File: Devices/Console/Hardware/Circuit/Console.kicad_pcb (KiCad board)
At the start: 2 copper layers, 96.8 x 60 mm, 30 parts, among them J1 AVR-ISP-6, J2 TYPE-C-31-M-12, J3 Conn_01x13, J4 Conn_01x04, J5 Conn_01x04, SW1 PEC11R-4220F-S0012, SW2 PEC11R-4220F-S0012, SW3 PEC11R-4220F-S0012, SW4 PEC11R-4220F-S0012, SW5 SW_Push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

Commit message: Finalize PCB
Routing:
- net BTN3: track 0.00 -> 291.0 mm, vias 0 -> 3
- net RST: track 0.00 -> 197.4 mm, vias 0 -> 6
- net GND: track 0.00 -> 178.3 mm, vias 0 -> 17
- net BTN1: track 0.00 -> 166.3 mm, vias 0 -> 7
- net VCC: track 0.00 -> 156.5 mm, vias 0 -> 8
- net BTN2: track 0.00 -> 151.6 mm, vias 0 -> 4
- net ENC4A: track 0.00 -> 106.2 mm, vias 0 -> 2
- net SCL: track 0.00 -> 101.4 mm, vias 0 -> 4
- net ENC4B: track 0.00 -> 93.7 mm
- net BTN4: track 0.00 -> 91.8 mm, vias 0 -> 5
- net SDA: track 0.00 -> 90.7 mm, vias 0 -> 8
- net ENC3A: track 0.00 -> 81.4 mm, vias 0 -> 2
- net ENC3B: track 0.00 -> 79.7 mm, vias 0 -> 4
- net RX: track 0.00 -> 74.1 mm, vias 0 -> 6
- net ENC2A: track 0.00 -> 67.8 mm, vias 0 -> 2
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- added copper zone on B.Cu, net GND
- added copper zone on F.Cu, net GND
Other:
- board text added: "GHOSCHT - 2021"
- board text added: "v01"

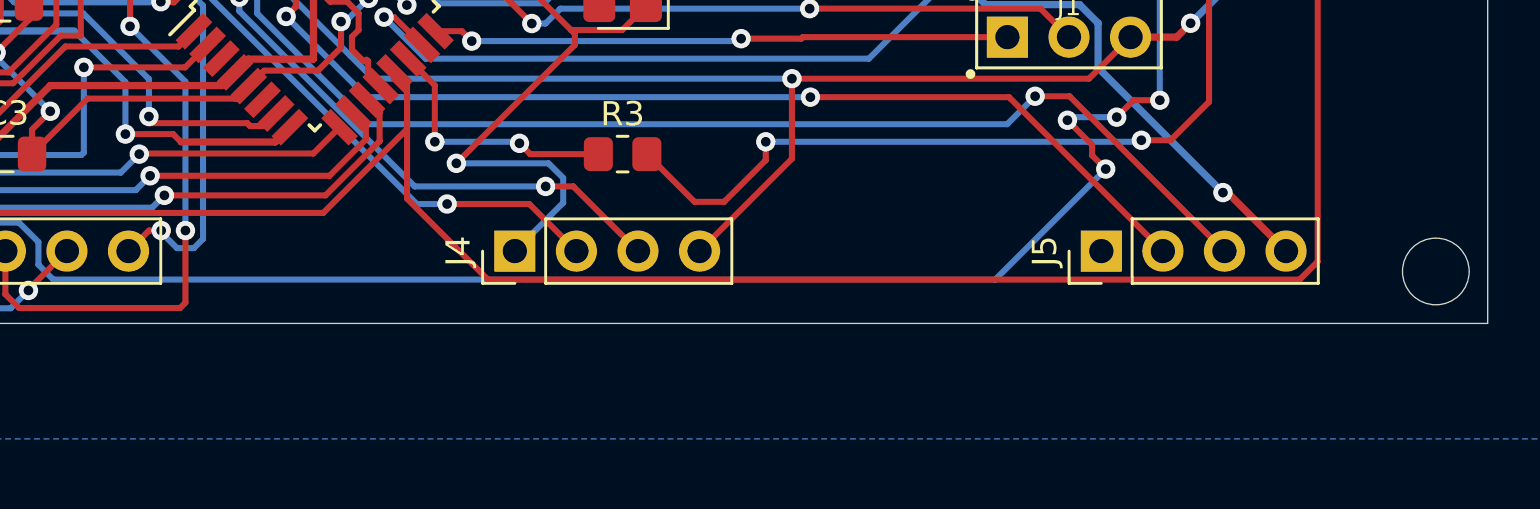
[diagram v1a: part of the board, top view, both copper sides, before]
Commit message: Add breakout pin description
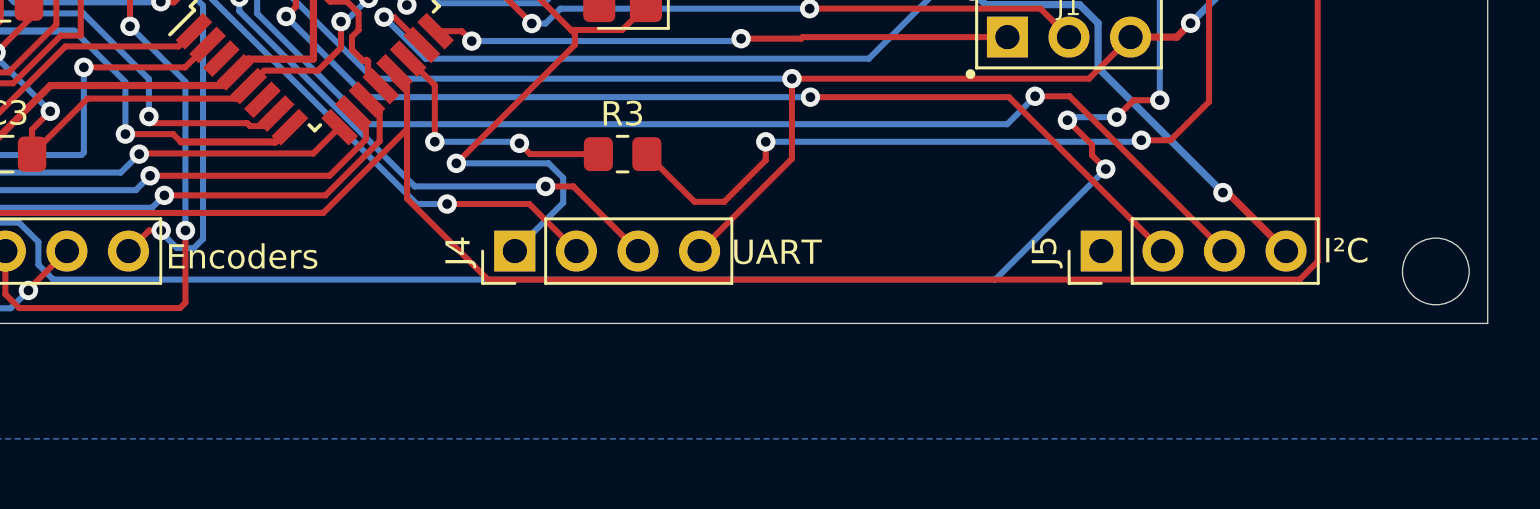
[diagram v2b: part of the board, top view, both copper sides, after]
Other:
- board text added: "Encoders"
- board text added: "I²C"
- board text added: "UART"
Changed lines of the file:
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@@
   (general
     (thickness 1.6)
-    (drawings 15)
+    (drawings 18)
     (tracks 833)
     (zones 0)
@@
     )
   )
+  (gr_text Encoders (at 143.256 122.047) (layer F.SilkS)
+    (effects (font (size 1 1) (thickness 0.15)))
+  )
+  (gr_text UART (at 165.2905 121.8565) (layer F.SilkS)
+    (effects (font (size 1 1) (thickness 0.15)))
+  )
+  (gr_text I²C (at 188.7855 121.793) (layer F.SilkS)
+    (effects (font (size 1 1) (thickness 0.15)))
+  )
   (gr_text "GHOSCHT - 2021" (at 192.913 113.4745 90) (layer B.SilkS)

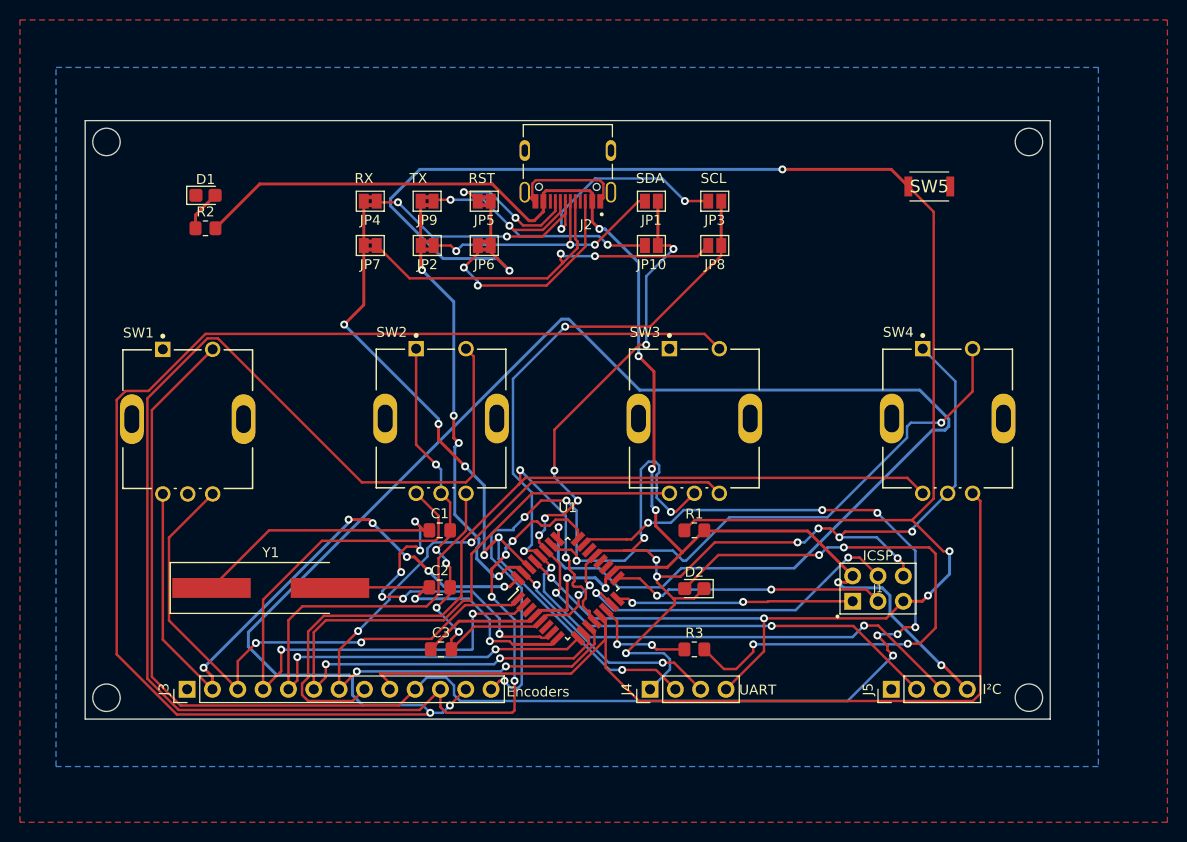
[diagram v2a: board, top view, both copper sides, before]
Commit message: Add proper mounting holes
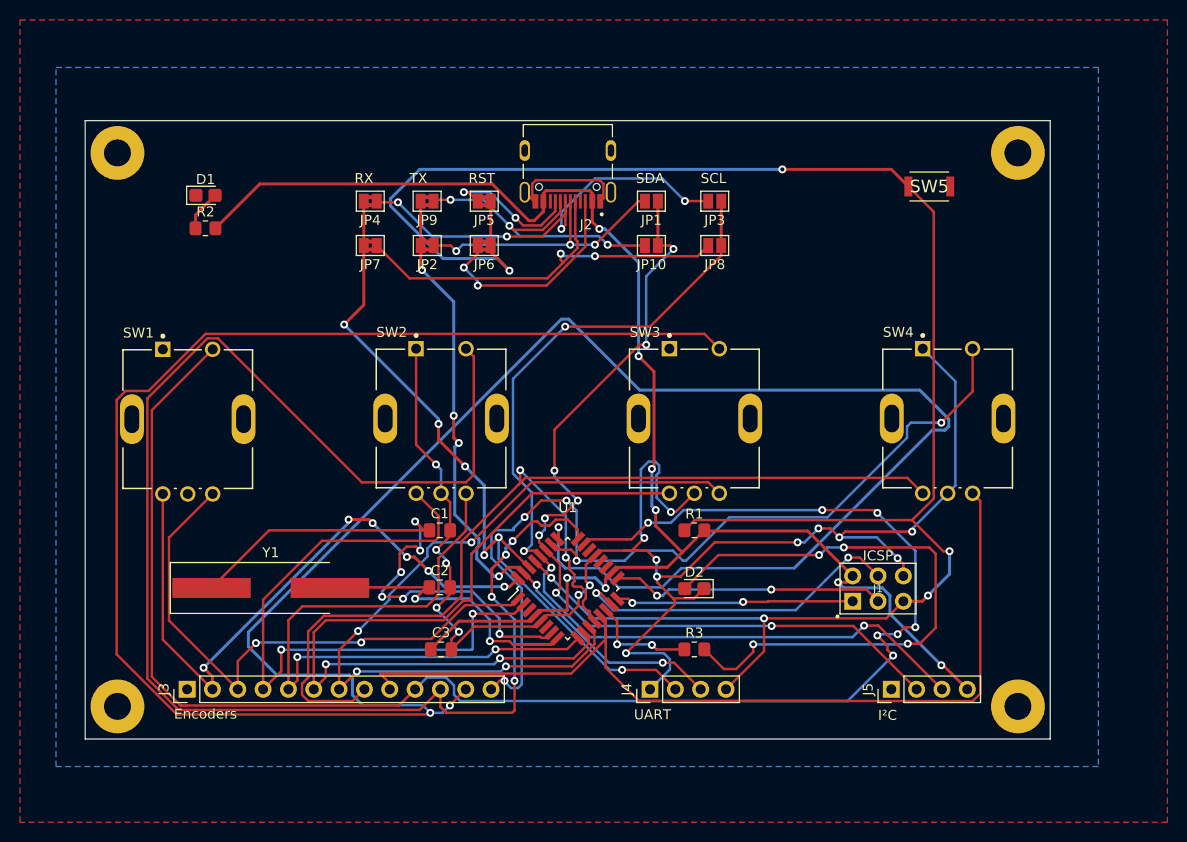
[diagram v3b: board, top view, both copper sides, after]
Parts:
- added PAD1: MountingHole_2.7mm_M2.5_Pad, MountingHole:MountingHole_2.7mm_M2.5_Pad, F.Cu at (101.1, 68.0)
- added PAD2: MountingHole_2.7mm_M2.5_Pad, MountingHole:MountingHole_2.7mm_M2.5_Pad, F.Cu at (191.4, 68.0)
- added PAD3: MountingHole_2.7mm_M2.5_Pad, MountingHole:MountingHole_2.7mm_M2.5_Pad, F.Cu at (101.1, 123.5)
- added PAD4: MountingHole_2.7mm_M2.5_Pad, MountingHole:MountingHole_2.7mm_M2.5_Pad, F.Cu at (191.4, 123.5)
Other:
- board size 96.8 x 60 mm -> 96.8 x 62 mm

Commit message: Improve routing with freerouting + manual fixes
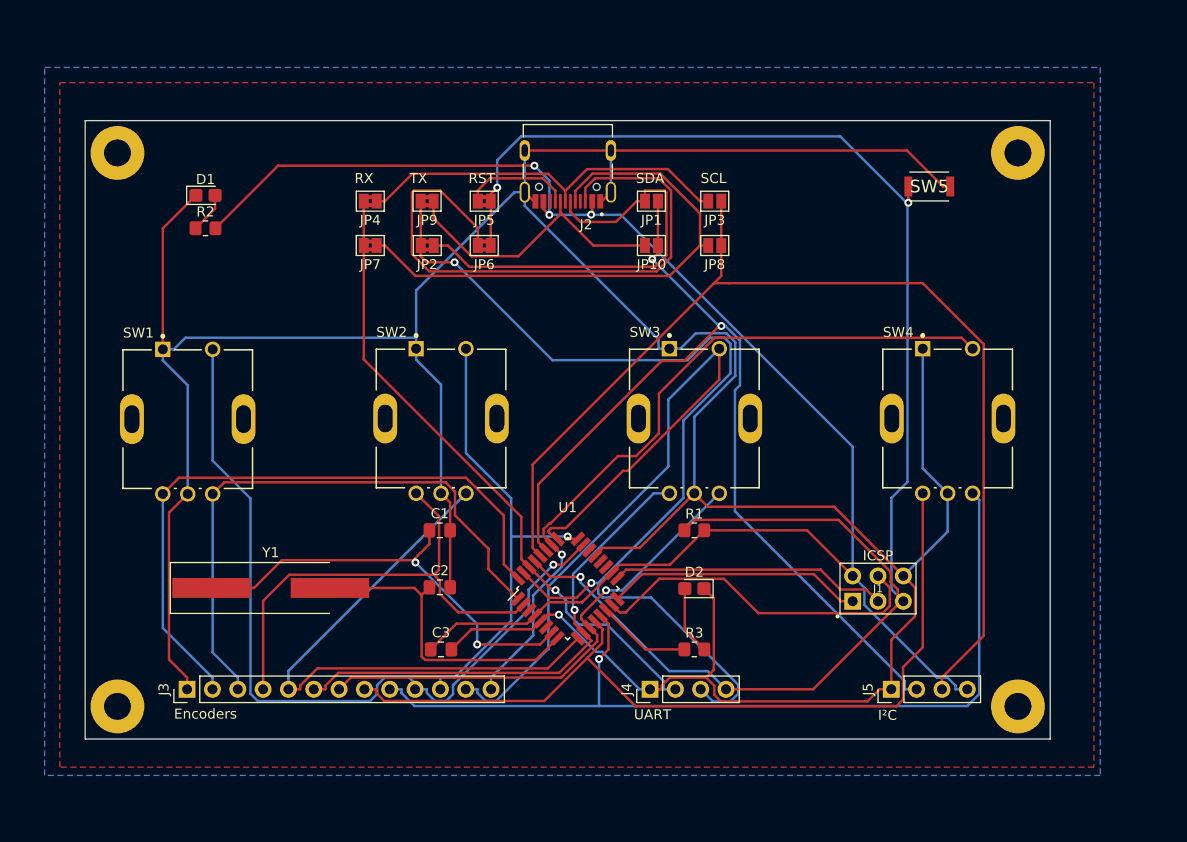
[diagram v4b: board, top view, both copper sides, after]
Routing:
- net BTN3: track 291.0 -> 76.2 mm, vias 3 -> 0
- net GND: track 178.3 -> 364.4 mm, vias 17 -> 1
- net BTN2: track 151.6 -> 46.6 mm, vias 4 -> 1
- net BTN1: track 166.3 -> 81.3 mm, vias 7 -> 1
- net Net-(D2-Pad2): track 60.7 -> 6.91 mm, vias 4 -> 0
- net Net-(J2-PadB8): track 22.1 -> 61.0 mm, vias 2 -> 0
- net TX: track 67.7 -> 105.1 mm, vias 6 -> 2
- net ENC3A: track 81.4 -> 50.5 mm, vias 2 -> 1
- net ENC3B: track 79.7 -> 50.1 mm, vias 4 -> 1
- net RST: track 197.4 -> 169.5 mm, vias 6 -> 3
- net ENC4A: track 106.2 -> 84.9 mm, vias 2 -> 0
- net ENC2A: track 67.8 -> 48.1 mm, vias 2 -> 0
- net BTN4: track 91.8 -> 73.5 mm, vias 5 -> 1
- net Net-(J2-PadA6): track 27.9 -> 44.1 mm, vias 3 -> 0
- net XTAL1: track 57.5 -> 44.1 mm, vias 6 -> 2
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
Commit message: Add additional decoupling capacitor
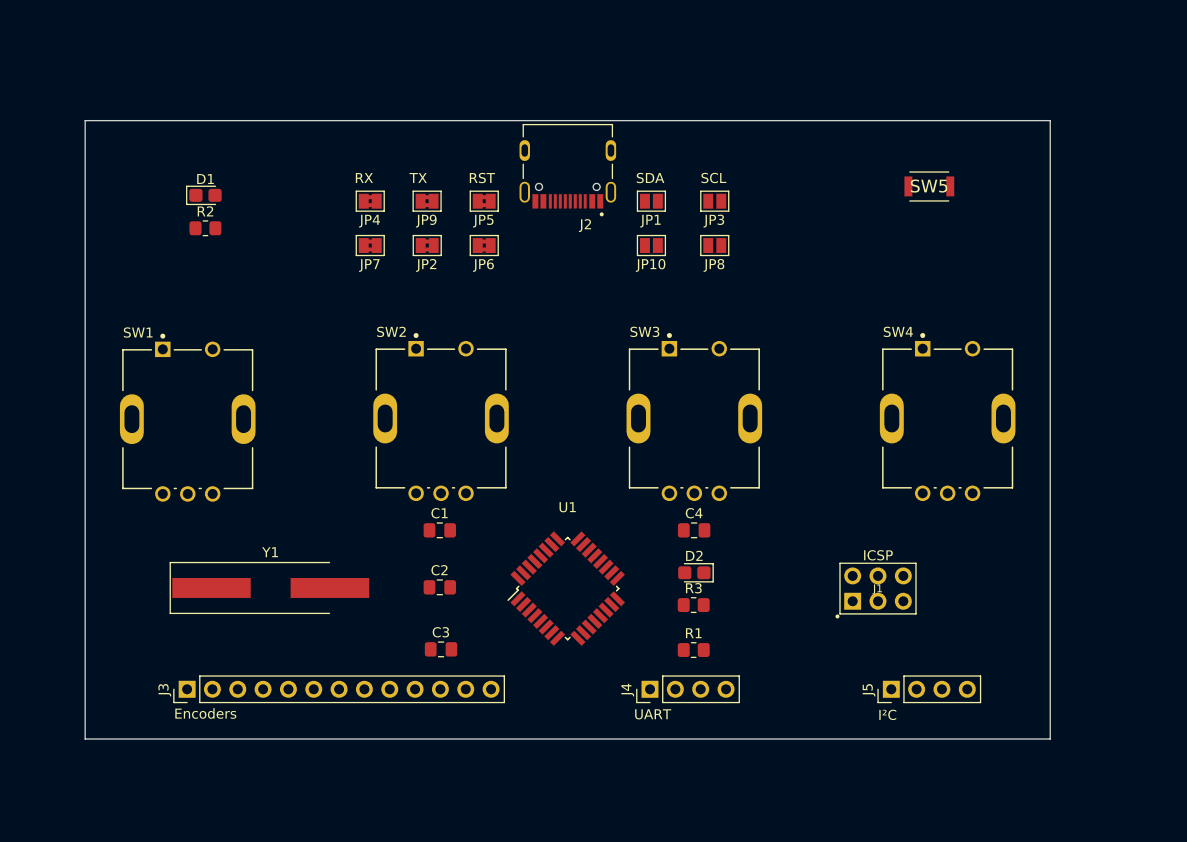
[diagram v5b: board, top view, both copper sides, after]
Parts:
- removed PAD1, PAD2, PAD3, PAD4: MountingHole_2.7mm_M2.5_Pad, MountingHole:MountingHole_2.7mm_M2.5_Pad
- added C4: 100n, Capacitor_SMD:C_0805_2012Metric_Pad1.18x1.45mm_HandSolder, F.Cu at (158.9, 105.9)
- moved R1 12.0 mm to (158.9, 117.9)
- moved R3 4.44 mm to (158.9, 113.3)
- moved D2 1.59 mm to (158.9, 110.1)
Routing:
- net GND: track 364.4 -> 0.00 mm, vias 1 -> 0
- net RST: track 169.5 -> 0.00 mm, vias 3 -> 0
- net VCC: track 162.7 -> 0.00 mm, vias 3 -> 0
- net SCL: track 109.6 -> 0.00 mm
- net TX: track 105.1 -> 0.00 mm, vias 2 -> 0
- net SDA: track 93.5 -> 0.00 mm, vias 2 -> 0
- net ENC4B: track 90.7 -> 0.00 mm, vias 1 -> 0
- net ENC4A: track 84.9 -> 0.00 mm
- net BTN1: track 81.3 -> 0.00 mm, vias 1 -> 0
- net BTN3: track 76.2 -> 0.00 mm
- net BTN4: track 73.5 -> 0.00 mm, vias 1 -> 0
- net ENC1A: track 65.0 -> 0.00 mm
- net RX: track 64.4 -> 0.00 mm, vias 1 -> 0
- net Net-(J2-PadB8): track 61.0 -> 0.00 mm
- net ENC1B: track 59.2 -> 0.00 mm
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- removed copper zone on B.Cu, net GND
- removed copper zone on F.Cu, net GND
